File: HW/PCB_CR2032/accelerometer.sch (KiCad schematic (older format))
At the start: 4 parts, among them U3 LIS2DW12

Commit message: * Updated Schematic with 1206 leds and 1k 0805 current limiting resistors
* Restored STDC14 and debug UART, now shared with top led of minute and second. Some other LED pins remapped

* Updated STM32CubeMX project to reflect schematic changes and generated code again
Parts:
- C13: Make Murata -> Yageo; Mouser 81-GRM21BR71A106KA73K -> 603-CC805KKX7R6BB106; Part GRM21BR71A106KA73K -> CC0805KKX7R6BB106
- C14: Make (none) -> Yageo; Mouser (none) -> 603-CC805KRX7R9BB104; Part (none) -> CC0805KRX7R9BB104
- D3: Make (none) -> ST; Mouser (none) -> 511-BAR43CFILM; Part (none) -> BAR43CFILM
- U3: Make (none) -> ST; Mouser (none) -> 511-LIS2DW12TR; Part (none) -> LIS2DW12TR
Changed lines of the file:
@@
 F 2 "Package_LGA:LGA-12_2x2mm_P0.5mm" H 3050 4050 50  0001 L CNN
 F 3 "www.st.com/resource/en/datasheet/lis2hh12.pdf" H 2550 3500 50  0001 C CNN
+F 4 "ST" H 2900 3500 50  0001 C CNN "Make"
+F 5 "511-LIS2DW12TR" H 2900 3500 50  0001 C CNN "Mouser"
+F 6 "LIS2DW12TR" H 2900 3500 50  0001 C CNN "Part"
 	1    2900 3500
 	1    0    0    -1
@@
 F 2 "Package_TO_SOT_SMD:SOT-23_Handsoldering" H 4500 3450 50  0001 C CNN
 F 3 "~" H 4500 3450 50  0001 C CNN
+F 4 "ST" H 4500 3450 50  0001 C CNN "Make"
+F 5 "511-BAR43CFILM" H 4500 3450 50  0001 C CNN "Mouser"
+F 6 "BAR43CFILM" H 4500 3450 50  0001 C CNN "Part"
 	1    4500 3450
 	0    -1   -1   0
@@
 F 2 "Capacitor_SMD:C_0805_2012Metric_Pad1.15x1.40mm_HandSolder" H 7988 1900 50  0001 C CNN
 F 3 "~" H 7950 2050 50  0001 C CNN
+F 4 "Yageo" H 7950 2050 50  0001 C CNN "Make"
+F 5 "603-CC805KRX7R9BB104" H 7950 2050 50  0001 C CNN "Mouser"
+F 6 "CC0805KRX7R9BB104" H 7950 2050 50  0001 C CNN "Part"
 	1    7950 2050
 	1    0    0    -1
@@
 F 2 "Capacitor_SMD:C_0805_2012Metric_Pad1.15x1.40mm_HandSolder" H 7288 1900 50  0001 C CNN
 F 3 "~" H 7250 2050 50  0001 C CNN
-F 4 "Murata" H 7250 2050 50  0001 C CNN "Make"
-F 5 "GRM21BR71A106KA73K" H 7250 2050 50  0001 C CNN "Part"
-F 6 "81-GRM21BR71A106KA73K" H 7250 2050 50  0001 C CNN "Mouser"
+F 4 "Yageo" H 7250 2050 50  0001 C CNN "Make"
+F 5 "CC0805KKX7R6BB106" H 7250 2050 50  0001 C CNN "Part"
+F 6 "603-CC805KKX7R6BB106" H 7250 2050 50  0001 C CNN "Mouser"
 	1    7250 2050
 	1    0    0    -1

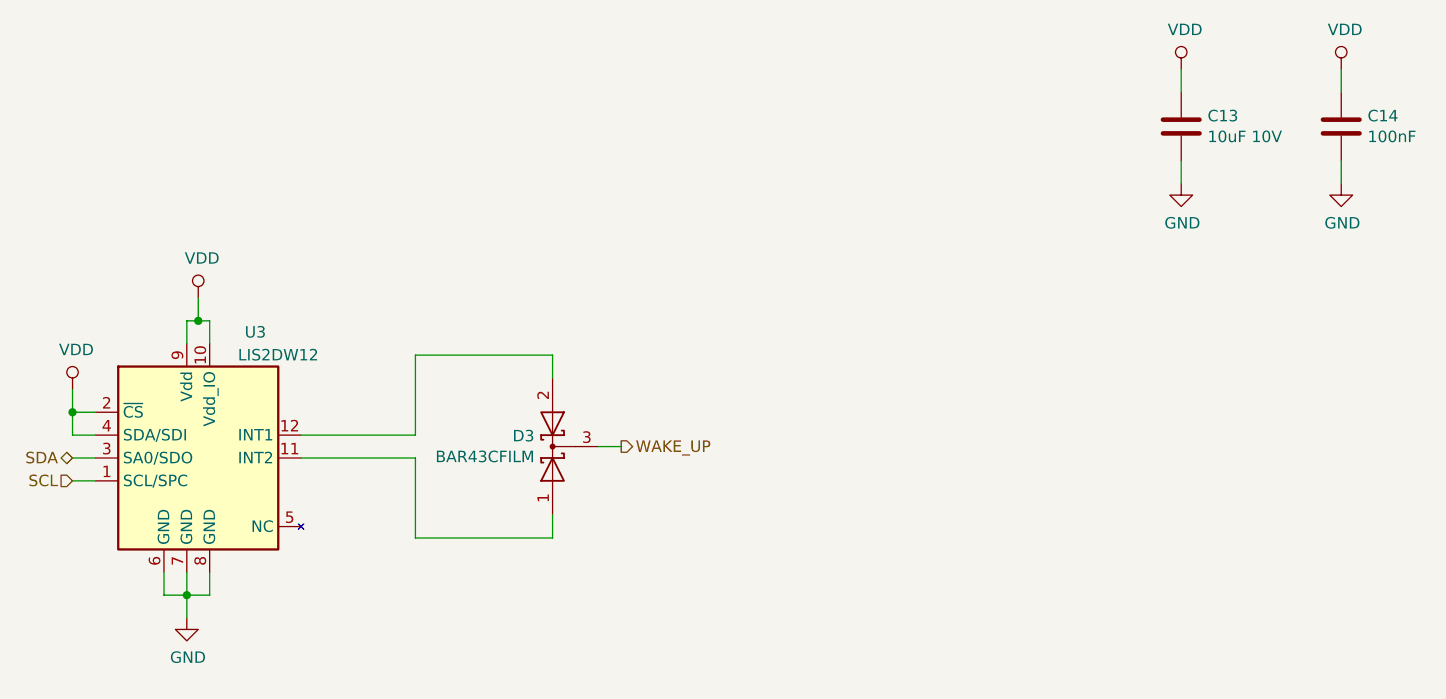
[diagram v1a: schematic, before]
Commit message: Created layout for CR2032 version 1.0, for first prototype order, resulted in a lot of changes in the pin-mapping to make routing easier.
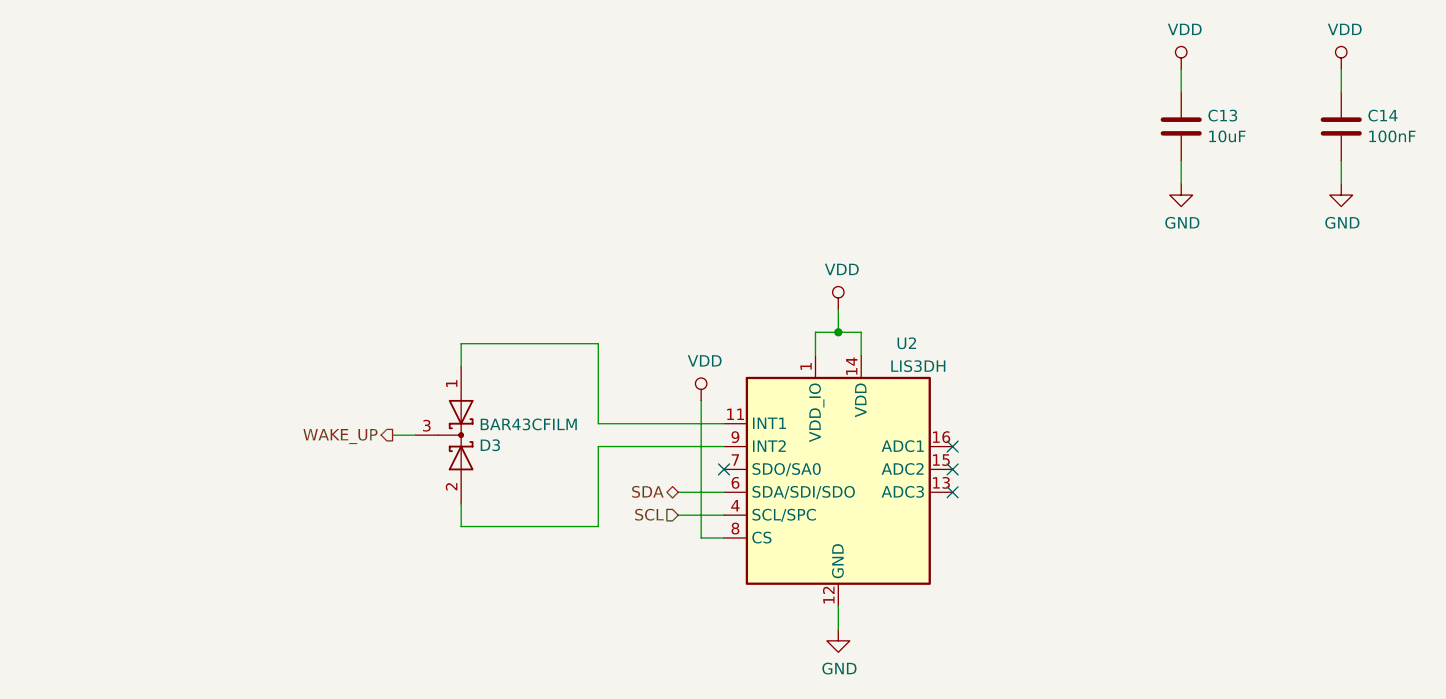
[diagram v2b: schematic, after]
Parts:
- removed U3: LIS2DW12, Package_LGA:LGA-12_2x2mm_P0.5mm, symbol PCB_CR2032:LIS2DW12
- added U2: LIS3DH, Package_LGA:LGA-16_3x3mm_P0.5mm_LayoutBorder3x5y, symbol Sensor_Motion:LIS3DH
- C13: value 10uF 10V -> 10uF; LCSC (none) -> C15850; Make Yageo -> (none); Mouser 603-CC805KKX7R6BB106 -> (none); Part CC0805KKX7R6BB106 -> (none); jlcpcb (none) -> CL21A106KAYNNNE
- C14: footprint Capacitor_SMD:C_0805_2012Metric_Pad1.15x1.40mm_HandSolder -> Capacitor_SMD:C_0603_1608Metric_Pad1.05x0.95mm_HandSolder; LCSC (none) -> C14663; Make Yageo -> (none); Mouser 603-CC805KRX7R9BB104 -> (none); Part CC0805KRX7R9BB104 -> (none); jlcpcb (none) -> CC0603KRX7R9BB104
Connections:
- net GND: now also U2.10 (GND), U2.12 (GND), U2.5 (GND)
- net SCL: now also U2.4 (SCL/SPC)
- net SDA: now also U2.6 (SDA/SDI/SDO)
- net VDD: now also U2.1 (VDD_IO), U2.14 (VDD), U2.8 (CS)
- net at D3.1 (A): now also U2.11 (INT1)
- net at D3.2 (A): now also U2.9 (INT2)
- no-connect marks 0 -> 4
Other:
- moved on the sheet: D3
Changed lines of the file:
@@
 Comment4 ""
 $EndDescr
-Text HLabel 2400 3600 0    50   Input ~ 0
+Text HLabel 5050 3750 0    50   Input ~ 0
 SCL
-Text HLabel 2400 3500 0    50   BiDi ~ 0
+Text HLabel 5050 3650 0    50   BiDi ~ 0
 SDA
-Text HLabel 4800 3450 2    50   Output ~ 0
+Text HLabel 3800 3400 0    50   Output ~ 0
 WAKE_UP
-$Comp
-L PCB_CR2032:LIS2DW12 U3
-U 1 1 5DC90EA6
-P 2900 3500
-F 0 "U3" H 3200 4050 50  0000 C CNN
-F 1 "LIS2DW12" H 3300 3950 50  0000 C CNN
-F 2 "Package_LGA:LGA-12_2x2mm_P0.5mm" H 3050 4050 50  0001 L CNN
-F 3 "www.st.com/resource/en/datasheet/lis2hh12.pdf" H 2550 3500 50  0001 C CNN
-F 4 "ST" H 2900 3500 50  0001 C CNN "Make"
-F 5 "511-LIS2DW12TR" H 2900 3500 50  0001 C CNN "Mouser"
-F 6 "LIS2DW12TR" H 2900 3500 50  0001 C CNN "Part"
-	1    2900 3500
-	1    0    0    -1
-$EndComp
-$Comp
-L Device:D_Schottky_x2_KCom_AAK D?
-U 1 1 5DCAA080
-P 4500 3450
-AR Path="/5DC4948F/5DCAA080" Ref="D?"  Part="1"
-AR Path="/5DC486A4/5DCAA080" Ref="D3"  Part="1"
-F 0 "D3" V 4546 3529 50  0000 L CNN
-F 1 "BAR43CFILM" V 4455 3529 50  0000 L CNN
-F 2 "Package_TO_SOT_SMD:SOT-23_Handsoldering" H 4500 3450 50  0001 C CNN
-F 3 "~" H 4500 3450 50  0001 C CNN
-F 4 "ST" H 4500 3450 50  0001 C CNN "Make"
-F 5 "511-BAR43CFILM" H 4500 3450 50  0001 C CNN "Mouser"
-F 6 "BAR43CFILM" H 4500 3450 50  0001 C CNN "Part"
-	1    4500 3450
-	0    -1   -1   0
-$EndComp
-Wire Wire Line
-	4700 3450 4800 3450
 $Comp
 L power:VDD #PWR028
 U 1 1 5DCAE2F8
-P 2950 2800
-F 0 "#PWR028" H 2950 2650 50  0001 C CNN
-F 1 "VDD" H 2967 2973 50  0000 C CNN
-F 2 "" H 2950 2800 50  0001 C CNN
-F 3 "" H 2950 2800 50  0001 C CNN
-	1    2950 2800
+P 5750 2850
+F 0 "#PWR028" H 5750 2700 50  0001 C CNN
+F 1 "VDD" H 5767 3023 50  0000 C CNN
+F 2 "" H 5750 2850 50  0001 C CNN
+F 3 "" H 5750 2850 50  0001 C CNN
+	1    5750 2850
 	1    0    0    -1
 $EndComp
@@
 L power:GND #PWR027
 U 1 1 5DCAEA47
-P 2900 4200
-F 0 "#PWR027" H 2900 3950 50  0001 C CNN
-F 1 "GND" H 2905 4027 50  0000 C CNN
-F 2 "" H 2900 4200 50  0001 C CNN
-F 3 "" H 2900 4200 50  0001 C CNN
-	1    2900 4200
-	1    0    0    -1
-$EndComp
-Wire Wire Line
-	2800 4000 2800 4100
-Wire Wire Line
-	2800 4100 2900 4100
-Wire Wire Line
-	3000 4100 3000 4000
-Wire Wire Line
-	2900 4000 2900 4100
-Connection ~ 2900 4100
-Wire Wire Line
-	2900 4100 3000 4100
-Wire Wire Line
-	2900 4100 2900 4200
-Wire Wire Line
-	2900 3000 2900 2900
-Wire Wire Line
-	2900 2900 2950 2900
-Wire Wire Line
-	3000 2900 3000 3000
-Wire Wire Line
-	2950 2900 2950 2800
-Connection ~ 2950 2900
-Wire Wire Line
-	2950 2900 3000 2900
+P 5750 4250
+F 0 "#PWR027" H 5750 4000 50  0001 C CNN
+F 1 "GND" H 5755 4077 50  0000 C CNN
+F 2 "" H 5750 4250 50  0001 C CNN
+F 3 "" H 5750 4250 50  0001 C CNN
+	1    5750 4250
+	1    0    0    -1
+$EndComp
 $Comp
 L power:VDD #PWR026
 U 1 1 5DCB1169
-P 2400 3200
-F 0 "#PWR026" H 2400 3050 50  0001 C CNN
-F 1 "VDD" H 2417 3373 50  0000 C CNN
-F 2 "" H 2400 3200 50  0001 C CNN
-F 3 "" H 2400 3200 50  0001 C CNN
-	1    2400 3200
-	1    0    0    -1
-$EndComp
-Wire Wire Line
-	2500 3300 2400 3300
-Wire Wire Line
-	2400 3300 2400 3200
-Wire Wire Line
-	2500 3400 2400 3400
-Wire Wire Line
-	2400 3400 2400 3300
-Connection ~ 2400 3300
-Wire Wire Line
-	2500 3500 2400 3500
-Wire Wire Line
-	2500 3600 2400 3600
-Wire Wire Line
-	3400 3400 3900 3400
-Wire Wire Line
-	3900 3400 3900 3050
-Wire Wire Line
-	3900 3050 4500 3050
-Wire Wire Line
-	4500 3050 4500 3150
-Wire Wire Line
-	3400 3500 3900 3500
-Wire Wire Line
-	3900 3500 3900 3850
-Wire Wire Line
-	3900 3850 4500 3850
-Wire Wire Line
-	4500 3850 4500 3750
+P 5150 3250
+F 0 "#PWR026" H 5150 3100 50  0001 C CNN
+F 1 "VDD" H 5167 3423 50  0000 C CNN
+F 2 "" H 5150 3250 50  0001 C CNN
+F 3 "" H 5150 3250 50  0001 C CNN
+	1    5150 3250
+	1    0    0    -1
+$EndComp
+Wire Wire Line
+	5250 3650 5050 3650
+Wire Wire Line
+	5250 3750 5050 3750
 $Comp
 L Device:C C?
@@
 F 0 "C14" H 8065 2096 50  0000 L CNN
 F 1 "100nF" H 8065 2005 50  0000 L CNN
-F 2 "Capacitor_SMD:C_0805_2012Metric_Pad1.15x1.40mm_HandSolder" H 7988 1900 50  0001 C CNN
+F 2 "Capacitor_SMD:C_0603_1608Metric_Pad1.05x0.95mm_HandSolder" H 7988 1900 50  0001 C CNN
 F 3 "~" H 7950 2050 50  0001 C CNN
-F 4 "Yageo" H 7950 2050 50  0001 C CNN "Make"
-F 5 "603-CC805KRX7R9BB104" H 7950 2050 50  0001 C CNN "Mouser"
-F 6 "CC0805KRX7R9BB104" H 7950 2050 50  0001 C CNN "Part"
+F 4 "" H 7950 2050 50  0001 C CNN "Make"
+F 5 "" H 7950 2050 50  0001 C CNN "Mouser"
+F 6 "" H 7950 2050 50  0001 C CNN "Part"
+F 7 "CC0603KRX7R9BB104" H 7950 2050 50  0001 C CNN "jlcpcb"
+F 8 "C14663" H 7950 2050 50  0001 C CNN "LCSC"
 	1    7950 2050
 	1    0    0    -1
@@
 AR Path="/5DC486A4/5DCB76B5" Ref="C13"  Part="1"
 F 0 "C13" H 7365 2096 50  0000 L CNN
-F 1 "10uF 10V" H 7365 2005 50  0000 L CNN
+F 1 "10uF" H 7365 2005 50  0000 L CNN
 F 2 "Capacitor_SMD:C_0805_2012Metric_Pad1.15x1.40mm_HandSolder" H 7288 1900 50  0001 C CNN
 F 3 "~" H 7250 2050 50  0001 C CNN
-F 4 "Yageo" H 7250 2050 50  0001 C CNN "Make"
-F 5 "CC0805KKX7R6BB106" H 7250 2050 50  0001 C CNN "Part"
-F 6 "603-CC805KKX7R6BB106" H 7250 2050 50  0001 C CNN "Mouser"
+F 4 "" H 7250 2050 50  0001 C CNN "Make"
+F 5 "" H 7250 2050 50  0001 C CNN "Part"
+F 6 "" H 7250 2050 50  0001 C CNN "Mouser"
+F 7 "CL21A106KAYNNNE" H 7250 2050 50  0001 C CNN "jlcpcb"
+F 8 "C15850" H 7250 2050 50  0001 C CNN "LCSC"
 	1    7250 2050
 	1    0    0    -1
@@
 Wire Wire Line
 	7950 1900 7950 1800
+$Comp
+L Sensor_Motion:LIS3DH U2
+U 1 1 5DD12756
+P 5750 3550
+F 0 "U2" H 6050 4100 50  0000 C CNN
+F 1 "LIS3DH" H 6100 4000 50  0000 C CNN
+F 2 "Package_LGA:LGA-16_3x3mm_P0.5mm_LayoutBorder3x5y" H 5850 2500 50  0001 C CNN
+F 3 "https://www.st.com/resource/en/datasheet/cd00274221.pdf" H 5550 3450 50  0001 C CNN
+F 4 "ST" H 5750 3550 50  0001 C CNN "Make"
+F 5 "LIS3DHTR" H 5750 3550 50  0001 C CNN "jlcpcb"
+F 6 "C15134" H 5750 3550 50  0001 C CNN "LCSC"
+	1    5750 3550
+	1    0    0    -1
+$EndComp
+Wire Wire Line
+	5650 3050 5650 2950
+Wire Wire Line
+	5650 2950 5750 2950
+Wire Wire Line
+	5850 2950 5850 3050
+Wire Wire Line
+	5750 2850 5750 2950
+Connection ~ 5750 2950
+Wire Wire Line
+	5750 2950 5850 2950
+Wire Wire Line
+	5150 3250 5150 3850
+Wire Wire Line
+	5150 3850 5250 3850
+Wire Wire Line
+	5750 4250 5750 4150
+Wire Wire Line
+	5250 3450 4700 3450
+Wire Wire Line
+	5250 3350 4700 3350
+$Comp
+L Device:D_Schottky_x2_KCom_AAK D?
+U 1 1 5DCAA080
+P 4100 3400
+AR Path="/5DC4948F/5DCAA080" Ref="D?"  Part="1"
+AR Path="/5DC486A4/5DCAA080" Ref="D3"  Part="1"
+F 0 "D3" V 4146 3479 50  0000 L CNN
+F 1 "BAR43CFILM" V 4055 3479 50  0000 L CNN
+F 2 "Package_TO_SOT_SMD:SOT-23_Handsoldering" H 4100 3400 50  0001 C CNN
+F 3 "~" H 4100 3400 50  0001 C CNN
+F 4 "ST" H 4100 3400 50  0001 C CNN "Make"
+F 5 "511-BAR43CFILM" H 4100 3400 50  0001 C CNN "Mouser"
+F 6 "BAR43CFILM" H 4100 3400 50  0001 C CNN "Part"
+	1    4100 3400
+	0    1    1    0
+$EndComp
+Wire Wire Line
+	3800 3400 3900 3400
+Wire Wire Line
+	4100 3100 4100 3000
+Wire Wire Line
+	4100 3000 4700 3000
+Wire Wire Line
+	4700 3000 4700 3350
+Wire Wire Line
+	4100 3700 4100 3800
+Wire Wire Line
+	4100 3800 4700 3800
+Wire Wire Line
+	4700 3450 4700 3800
+NoConn ~ 6250 3450
+NoConn ~ 6250 3550
+NoConn ~ 6250 3650
+NoConn ~ 5250 3550
 $EndSCHEMATC

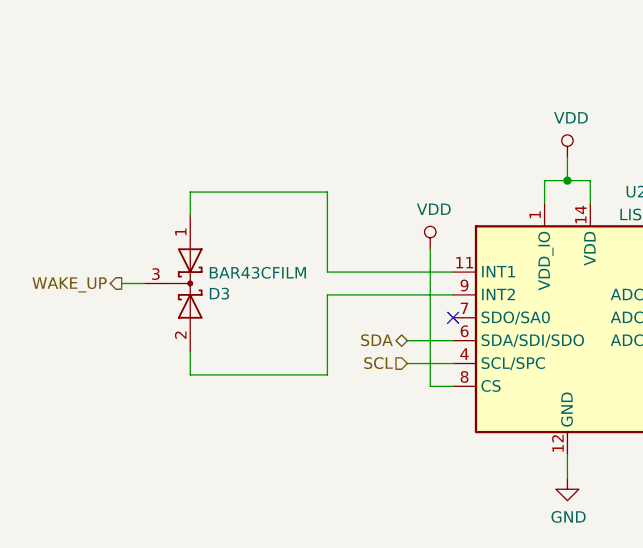
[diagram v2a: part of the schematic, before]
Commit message: Worked on Rev 2.0 HW with smaller size.
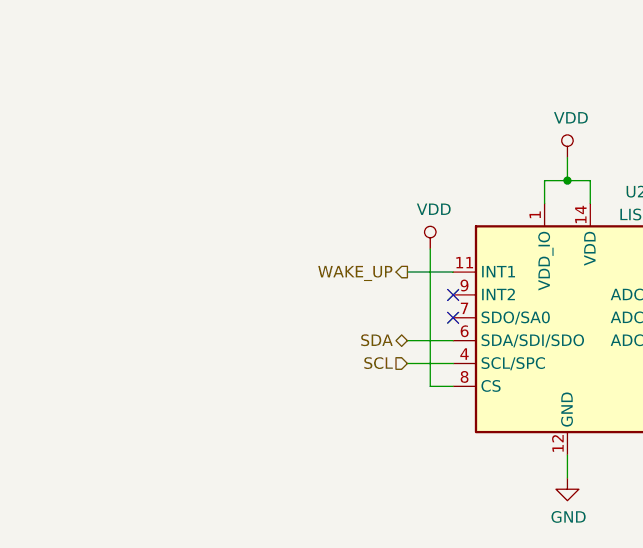
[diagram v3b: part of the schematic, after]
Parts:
- removed D3: BAR43CFILM, Package_TO_SOT_SMD:SOT-23_Handsoldering, symbol Device:D_Schottky_x2_KCom_AAK
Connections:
- net WAKE_UP: now also U2.11 (INT1)
- no-connect marks 4 -> 5
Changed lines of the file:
@@
 Text HLabel 5050 3650 0    50   BiDi ~ 0
 SDA
-Text HLabel 3800 3400 0    50   Output ~ 0
+Text HLabel 5050 3350 0    50   Output ~ 0
 WAKE_UP
 $Comp
@@
 Wire Wire Line
 	5750 4250 5750 4150
-Wire Wire Line
-	5250 3450 4700 3450
-Wire Wire Line
-	5250 3350 4700 3350
-$Comp
-L Device:D_Schottky_x2_KCom_AAK D?
-U 1 1 5DCAA080
-P 4100 3400
-AR Path="/5DC4948F/5DCAA080" Ref="D?"  Part="1"
-AR Path="/5DC486A4/5DCAA080" Ref="D3"  Part="1"
-F 0 "D3" V 4146 3479 50  0000 L CNN
-F 1 "BAR43CFILM" V 4055 3479 50  0000 L CNN
-F 2 "Package_TO_SOT_SMD:SOT-23_Handsoldering" H 4100 3400 50  0001 C CNN
-F 3 "~" H 4100 3400 50  0001 C CNN
-F 4 "ST" H 4100 3400 50  0001 C CNN "Make"
-F 5 "511-BAR43CFILM" H 4100 3400 50  0001 C CNN "Mouser"
-F 6 "BAR43CFILM" H 4100 3400 50  0001 C CNN "Part"
-	1    4100 3400
-	0    1    1    0
-$EndComp
-Wire Wire Line
-	3800 3400 3900 3400
-Wire Wire Line
-	4100 3100 4100 3000
-Wire Wire Line
-	4100 3000 4700 3000
-Wire Wire Line
-	4700 3000 4700 3350
-Wire Wire Line
-	4100 3700 4100 3800
-Wire Wire Line
-	4100 3800 4700 3800
-Wire Wire Line
-	4700 3450 4700 3800
 NoConn ~ 6250 3450
 NoConn ~ 6250 3550
 NoConn ~ 6250 3650
 NoConn ~ 5250 3550
+Wire Wire Line
+	5250 3350 5050 3350
+NoConn ~ 5250 3450
 $EndSCHEMATC

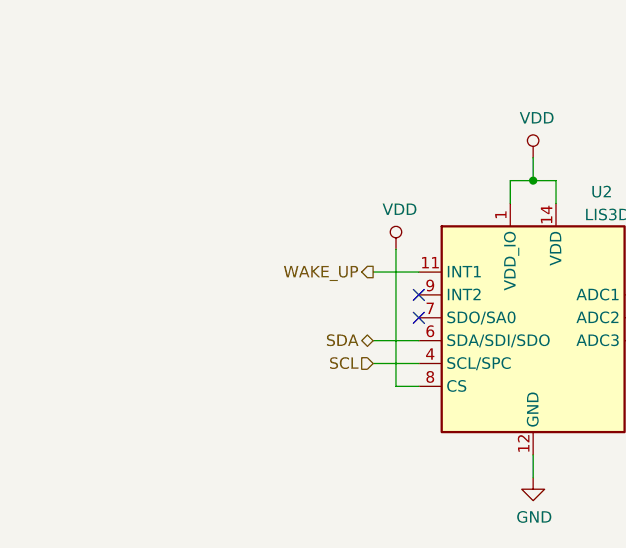
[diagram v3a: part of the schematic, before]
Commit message: Worked some more on rev 2.0 schematic. Almost done! Also added 3D-model of battery holder to library.
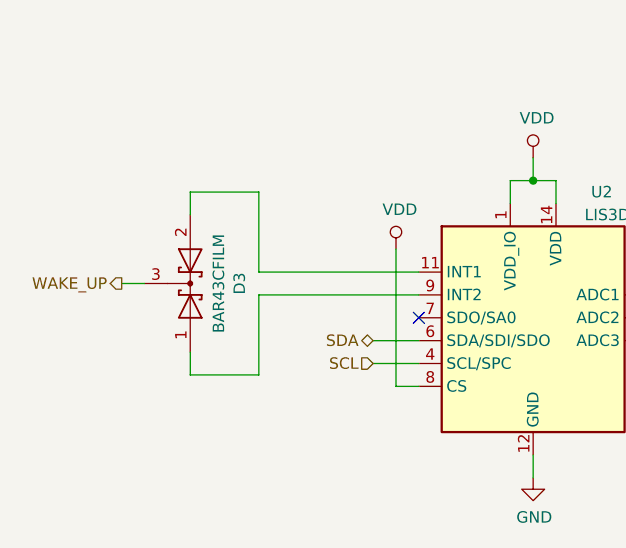
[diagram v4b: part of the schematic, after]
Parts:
- added D3: BAR43CFILM, Package_TO_SOT_SMD:SOT-23_Handsoldering, symbol Device:D_Schottky_x2_KCom_AAK
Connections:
- net WAKE_UP: now also D3.3 (K); no longer U2.11 (INT1)
- net at U2.9 (INT2): now also D3.1 (A)
- new net: D3.2 (A), U2.11 (INT1)
- no-connect marks 5 -> 4
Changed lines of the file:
@@
 Text HLabel 5050 3650 0    50   BiDi ~ 0
 SDA
-Text HLabel 5050 3350 0    50   Output ~ 0
+Text HLabel 3950 3400 0    50   Output ~ 0
 WAKE_UP
 $Comp
@@
 NoConn ~ 6250 3650
 NoConn ~ 5250 3550
-Wire Wire Line
-	5250 3350 5050 3350
-NoConn ~ 5250 3450
+$Comp
+L Device:D_Schottky_x2_KCom_AAK D?
+U 1 1 5DCE1B1E
+P 4250 3400
+AR Path="/5DC4948F/5DCE1B1E" Ref="D?"  Part="1"
+AR Path="/5DC486A4/5DCE1B1E" Ref="D3"  Part="1"
+F 0 "D3" H 4250 3616 50  0000 C CNN
+F 1 "BAR43CFILM" H 4250 3525 50  0000 C CNN
+F 2 "Package_TO_SOT_SMD:SOT-23_Handsoldering" H 4250 3400 50  0001 C CNN
+F 3 "~" H 4250 3400 50  0001 C CNN
+F 4 "ST" H 4250 3400 50  0001 C CNN "Make"
+F 5 "511-BAR43CFILM" H 4250 3400 50  0001 C CNN "Mouser"
+F 6 "BAR43CFILM" H 4250 3400 50  0001 C CNN "Part"
+	1    4250 3400
+	0    1    -1   0
+$EndComp
+Wire Wire Line
+	4550 3450 4550 3800
+Wire Wire Line
+	4550 3800 4250 3800
+Wire Wire Line
+	4250 3800 4250 3700
+Wire Wire Line
+	4550 3450 5250 3450
+Wire Wire Line
+	4550 3350 4550 3000
+Wire Wire Line
+	4550 3000 4250 3000
+Wire Wire Line
+	4250 3000 4250 3100
+Wire Wire Line
+	4550 3350 5250 3350
+Wire Wire Line
+	4050 3400 3950 3400
 $EndSCHEMATC
